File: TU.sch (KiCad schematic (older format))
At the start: 8 parts

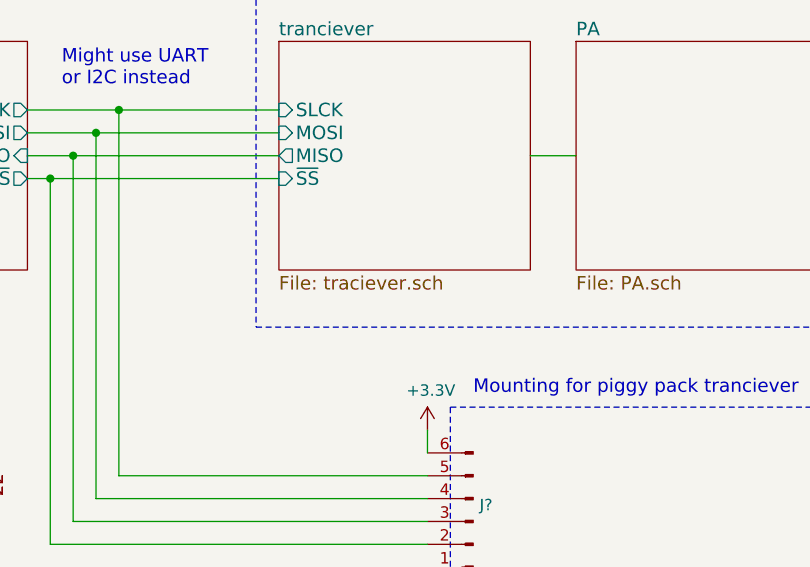
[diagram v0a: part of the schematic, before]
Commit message: Imported CAN and PSU blocks from infrastructure rep
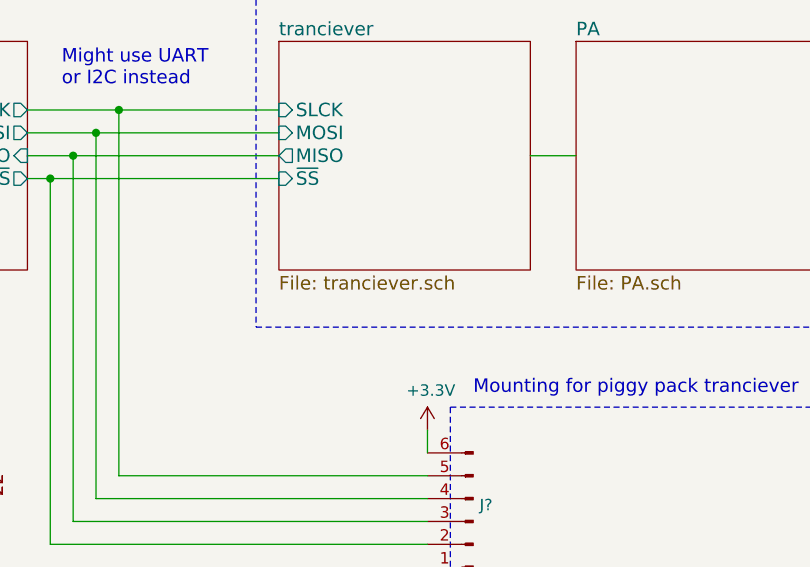
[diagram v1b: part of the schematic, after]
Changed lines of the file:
@@
 EESchema Schematic File Version 4
+LIBS:TU-cache
 EELAYER 30 0
 EELAYER END
@@
 $EndComp
 $Sheet
-S 6000 3000 1100 1000
-U 60144969
-F0 "tranciever" 59
-F1 "traciever.sch" 59
-F2 "SLCK" I L 6000 3300 59
-F3 "MOSI" I L 6000 3400 59
-F4 "MISO" O L 6000 3500 59
-F5 "~SS" I L 6000 3600 59
-$EndSheet
-$Sheet
 S 7300 3000 1100 1000
 U 60144AA2
@@
 Wire Wire Line
 	5100 3500 4900 3500
-Connection ~ 5000 3600
 Wire Wire Line
 	5000 3600 4900 3600
@@
 Wire Wire Line
 	5100 3500 6000 3500
-Wire Wire Line
-	5000 3600 6000 3600
 Wire Notes Line
 	5900 2650 5900 4250
@@
 Wire Notes Line
 	5900 2650 8550 2650
+$Sheet
+S 6000 3000 1100 1000
+U 60144374
+F0 "tranciever" 59
+F1 "tranciever.sch" 59
+F2 "SLCK" I L 6000 3300 59
+F3 "MOSI" I L 6000 3400 59
+F4 "MISO" O L 6000 3500 59
+F5 "~SS" I L 6000 3600 59
+$EndSheet
 Text Notes 5900 2600 0    59   ~ 0
 RF front end\n
+Connection ~ 5000 3600
+Wire Wire Line
+	5000 3600 6000 3600
 $EndSCHEMATC

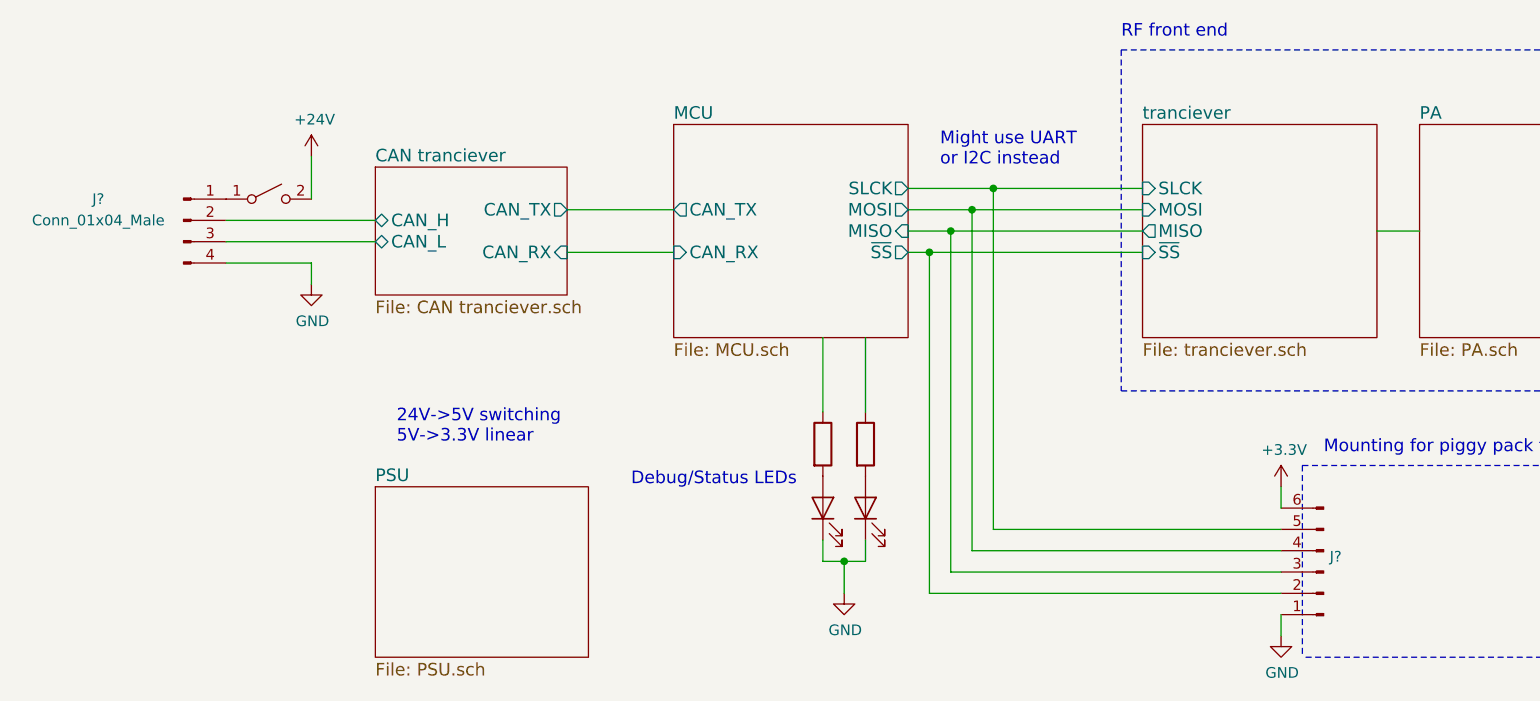
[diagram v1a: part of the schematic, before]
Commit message: Fixed weird hierarchical sheets
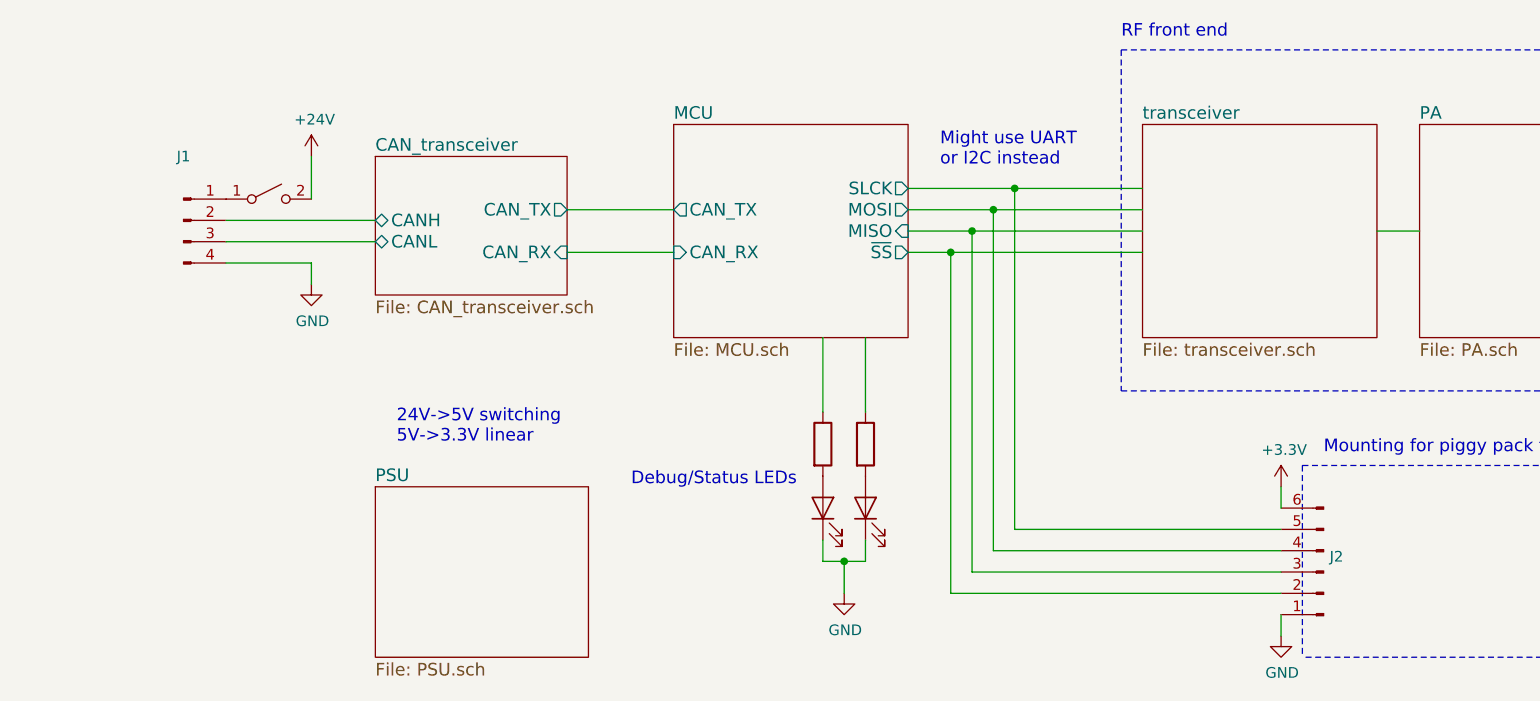
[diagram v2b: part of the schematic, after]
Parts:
- gave numbers to parts that had none: 8
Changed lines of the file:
@@
 	9100 3500 9100 3300
 $Comp
-L Device:Antenna AE?
+L Device:Antenna AE1
 U 1 1 60144042
 P 9100 3100
-F 0 "AE?" H 9180 3089 50  0001 L CNN
+F 0 "AE1" H 9180 3089 50  0001 L CNN
 F 1 "Antenna" H 9180 3043 50  0000 L CNN
 F 2 "" H 9100 3100 50  0001 C CNN
@@
 	1    0    0    -1
 $EndComp
-$Sheet
-S 7300 3000 1100 1000
-U 60144AA2
-F0 "PA" 59
-F1 "PA.sch" 59
-$EndSheet
 $Sheet
 S 3800 3000 1100 1000
@@
 F7 "CAN_RX" I L 3800 3600 59
 $EndSheet
-$Sheet
-S 2400 3200 900  600
-U 601450C1
-F0 "CAN tranciever" 59
-F1 "CAN tranciever.sch" 59
-F2 "CAN_H" B L 2400 3450 59
-F3 "CAN_L" B L 2400 3550 59
-F4 "CAN_TX" O R 3300 3400 59
-F5 "CAN_RX" I R 3300 3600 59
-$EndSheet
 Wire Wire Line
 	3300 3400 3800 3400
@@
 $EndSheet
 $Comp
-L Connector:Conn_01x04_Male J?
+L Connector:Conn_01x04_Male J1
 U 1 1 60145E85
 P 1500 3450
-F 0 "J?" H 1100 3550 50  0000 C CNN
-F 1 "Conn_01x04_Male" H 1100 3450 50  0000 C CNN
+F 0 "J1" H 1500 3750 50  0000 C CNN
+F 1 "Conn_01x04_Male" H 1100 3450 50  0001 C CNN
 F 2 "" H 1500 3450 50  0001 C CNN
 F 3 "~" H 1500 3450 50  0001 C CNN
@@
 $EndComp
 $Comp
-L Connector:Conn_01x06_Male J?
+L Connector:Conn_01x06_Male J2
 U 1 1 601485C2
 P 6850 5100
-F 0 "J?" H 6822 5028 50  0000 R CNN
+F 0 "J2" H 6822 5028 50  0000 R CNN
 F 1 "Conn_01x06_Male" H 6822 5073 50  0001 R CNN
 F 2 "" H 6850 5100 50  0001 C CNN
@@
 Text Notes 6850 4550 0    59   ~ 0
 Mounting for piggy pack tranciever
-Wire Wire Line
-	4900 3300 5300 3300
-Connection ~ 5300 3300
-Connection ~ 5200 3400
-Wire Wire Line
-	5200 3400 4900 3400
-Connection ~ 5100 3500
-Wire Wire Line
-	5100 3500 4900 3500
-Wire Wire Line
-	5000 3600 4900 3600
-$Comp
-L power:GND #PWR?
+$Comp
+L power:GND #PWR0101
 U 1 1 6014B5F8
 P 6650 5400
-F 0 "#PWR?" H 6650 5150 50  0001 C CNN
+F 0 "#PWR0101" H 6650 5150 50  0001 C CNN
 F 1 "GND" H 6655 5227 50  0000 C CNN
 F 2 "" H 6650 5400 50  0001 C CNN
@@
 $EndComp
 $Comp
-L power:+3.3V #PWR?
+L power:+3.3V #PWR0102
 U 1 1 6014B909
 P 6650 4700
-F 0 "#PWR?" H 6650 4550 50  0001 C CNN
+F 0 "#PWR0102" H 6650 4550 50  0001 C CNN
 F 1 "+3.3V" H 6665 4873 50  0000 C CNN
 F 2 "" H 6650 4700 50  0001 C CNN
@@
 	8400 3500 9100 3500
 Wire Wire Line
-	5300 3300 5300 4900
-Wire Wire Line
-	5300 4900 6650 4900
-Wire Wire Line
-	5200 3400 5200 5000
-Wire Wire Line
-	5200 5000 6650 5000
-Wire Wire Line
-	5100 3500 5100 5100
-Wire Wire Line
-	5100 5100 6650 5100
-Wire Wire Line
-	5000 5200 6650 5200
-Wire Wire Line
-	5000 3600 5000 5200
-$Comp
-L power:+24V #PWR?
+	5400 3300 5400 4900
+$Comp
+L power:+24V #PWR0103
 U 1 1 6015CE4B
 P 2100 3150
-F 0 "#PWR?" H 2100 3000 50  0001 C CNN
+F 0 "#PWR0103" H 2100 3000 50  0001 C CNN
 F 1 "+24V" H 2115 3323 50  0000 C CNN
 F 2 "" H 2100 3150 50  0001 C CNN
@@
 	2100 3650 2100 3750
 $Comp
-L power:GND #PWR?
+L power:GND #PWR0104
 U 1 1 6015D658
 P 2100 3750
-F 0 "#PWR?" H 2100 3500 50  0001 C CNN
+F 0 "#PWR0104" H 2100 3500 50  0001 C CNN
 F 1 "GND" H 2105 3577 50  0000 C CNN
 F 2 "" H 2100 3750 50  0001 C CNN
@@
 Debug/Status LEDs
 $Comp
-L power:GND #PWR?
+L power:GND #PWR0105
 U 1 1 6016E9C7
 P 4600 5200
-F 0 "#PWR?" H 4600 4950 50  0001 C CNN
+F 0 "#PWR0105" H 4600 4950 50  0001 C CNN
 F 1 "GND" H 4605 5027 50  0000 C CNN
 F 2 "" H 4600 5200 50  0001 C CNN
@@
 $EndComp
 $Comp
-L Device:LED D?
+L Device:LED D1
 U 1 1 601771CD
 P 4500 4800
-F 0 "D?" V 4539 4683 50  0001 R CNN
+F 0 "D1" V 4539 4683 50  0001 R CNN
 F 1 "LED" V 4448 4683 50  0001 R CNN
 F 2 "" H 4500 4800 50  0001 C CNN
@@
 $EndComp
 $Comp
-L Device:LED D?
+L Device:LED D2
 U 1 1 601777B4
 P 4700 4800
-F 0 "D?" V 4739 4683 50  0001 R CNN
+F 0 "D2" V 4739 4683 50  0001 R CNN
 F 1 "LED" V 4648 4683 50  0001 R CNN
 F 2 "" H 4700 4800 50  0001 C CNN
@@
 $EndComp
 $Comp
-L Device:R R?
+L Device:R R1
 U 1 1 60178366
 P 4500 4500
-F 0 "R?" H 4570 4546 50  0001 L CNN
+F 0 "R1" H 4570 4546 50  0001 L CNN
 F 1 "R" H 4570 4455 50  0001 L CNN
 F 2 "" V 4430 4500 50  0001 C CNN
@@
 $EndComp
 $Comp
-L Device:R R?
+L Device:R R2
 U 1 1 601786A2
 P 4700 4500
-F 0 "R?" H 4770 4546 50  0001 L CNN
+F 0 "R2" H 4770 4546 50  0001 L CNN
 F 1 "R" H 4770 4455 50  0001 L CNN
 F 2 "" V 4630 4500 50  0001 C CNN
@@
 	4500 4000 4500 4350
 $Comp
-L Switch:SW_DPST_x2 SW?
+L Switch:SW_DPST_x2 SW1
 U 1 1 6018598A
 P 1900 3350
-F 0 "SW?" H 1900 3585 50  0001 C CNN
+F 0 "SW1" H 1900 3585 50  0001 C CNN
 F 1 "SW_DPST_x2" H 1900 3494 50  0001 C CNN
 F 2 "" H 1900 3350 50  0000 C CNN
@@
 Wire Wire Line
 	7100 3500 7300 3500
-Wire Wire Line
-	5300 3300 6000 3300
-Wire Wire Line
-	5200 3400 6000 3400
-Wire Wire Line
-	5100 3500 6000 3500
 Wire Notes Line
 	5900 2650 5900 4250
@@
 Wire Notes Line
 	5900 2650 8550 2650
-$Sheet
-S 6000 3000 1100 1000
-U 60144374
-F0 "tranciever" 59
-F1 "tranciever.sch" 59
-F2 "SLCK" I L 6000 3300 59
-F3 "MOSI" I L 6000 3400 59
-F4 "MISO" O L 6000 3500 59
-F5 "~SS" I L 6000 3600 59
-$EndSheet
 Text Notes 5900 2600 0    59   ~ 0
 RF front end\n
-Connection ~ 5000 3600
-Wire Wire Line
-	5000 3600 6000 3600
+$Sheet
+S 6000 3000 1100 1000
+U 60145F44
+F0 "transceiver" 59
+F1 "transceiver.sch" 59
+$EndSheet
+$Sheet
+S 7300 3000 1100 1000
+U 6014566F
+F0 "PA" 59
+F1 "PA.sch" 59
+$EndSheet
+$Sheet
+S 2400 3150 900  650
+U 60145813
+F0 "CAN_transceiver" 59
+F1 "CAN_transceiver.sch" 59
+F2 "CAN_TX" O R 3300 3400 59
+F3 "CAN_RX" I R 3300 3600 59
+F4 "CANH" B L 2400 3450 59
+F5 "CANL" B L 2400 3550 59
+$EndSheet
+Connection ~ 5100 3600
+Wire Wire Line
+	5100 3600 6000 3600
+Wire Wire Line
+	5100 5200 6650 5200
+Connection ~ 5200 3500
+Wire Wire Line
+	5200 3500 6000 3500
+Wire Wire Line
+	5200 5100 6650 5100
+Connection ~ 5300 3400
+Wire Wire Line
+	5300 3400 6000 3400
+Wire Wire Line
+	5300 5000 6650 5000
+Connection ~ 5400 3300
+Wire Wire Line
+	5400 3300 6000 3300
+Wire Wire Line
+	5400 4900 6650 4900
+Wire Wire Line
+	4900 3300 5400 3300
+Wire Wire Line
+	4900 3400 5300 3400
+Wire Wire Line
+	4900 3500 5200 3500
+Wire Wire Line
+	4900 3600 5100 3600
+Wire Wire Line
+	5100 3600 5100 5200
+Wire Wire Line
+	5200 3500 5200 5100
+Wire Wire Line
+	5300 3400 5300 5000
 $EndSCHEMATC

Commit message: Added cc1190 reference design
also changed cc1190 symbol
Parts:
- removed AE1: Antenna, symbol Device:Antenna
- added J3: Conn_Coaxial, symbol Connector:Conn_Coaxial
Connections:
- wire segments 35 -> 33
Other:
- note added: "SMA antenna connector"
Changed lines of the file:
@@
 Comment4 ""
 $EndDescr
-Wire Wire Line
-	9100 3500 9100 3300
-$Comp
-L Device:Antenna AE1
-U 1 1 60144042
-P 9100 3100
-F 0 "AE1" H 9180 3089 50  0001 L CNN
-F 1 "Antenna" H 9180 3043 50  0000 L CNN
-F 2 "" H 9100 3100 50  0001 C CNN
-F 3 "~" H 9100 3100 50  0001 C CNN
-	1    9100 3100
-	1    0    0    -1
-$EndComp
 $Sheet
 S 3800 3000 1100 1000
@@
 Text Notes 5050 3200 0    59   ~ 0
 Might use UART \nor I2C instead
-Wire Wire Line
-	7100 3500 7300 3500
 Wire Notes Line
 	5900 2650 5900 4250
@@
 S 7300 3000 1100 1000
 U 6014566F
-F0 "PA" 59
+F0 "CC1190" 59
 F1 "PA.sch" 59
+F2 "HGM" I L 7300 3250 39
+F3 "LNA_EN" I L 7300 3350 39
+F4 "PA_EN" I L 7300 3450 39
+F5 "RFIO" B L 7300 3550 39
+F6 "ANTENNA_OUT" O R 8400 3500 39
 $EndSheet
 $Sheet
@@
 Wire Wire Line
 	5300 3400 5300 5000
+$Comp
+L Connector:Conn_Coaxial J3
+U 1 1 60221CCA
+P 9300 3500
+F 0 "J3" H 9400 3475 50  0000 L CNN
+F 1 "Conn_Coaxial" H 9400 3384 50  0000 L CNN
+F 2 "" H 9300 3500 50  0001 C CNN
+F 3 " ~" H 9300 3500 50  0001 C CNN
+	1    9300 3500
+	1    0    0    -1
+$EndComp
+$Comp
+L power:GND #PWR01
+U 1 1 60222AF8
+P 9300 3700
+F 0 "#PWR01" H 9300 3450 50  0001 C CNN
+F 1 "GND" H 9305 3527 50  0000 C CNN
+F 2 "" H 9300 3700 50  0001 C CNN
+F 3 "" H 9300 3700 50  0001 C CNN
+	1    9300 3700
+	1    0    0    -1
+$EndComp
+Text Notes 8850 3300 0    59   ~ 0
+SMA antenna connector
 $EndSCHEMATC

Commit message: Started work on CC1200
might not be actual final tranciever
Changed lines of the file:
@@
 F3 "MOSI" O R 4900 3400 59
 F4 "MISO" I R 4900 3500 59
-F5 "~SS" O R 4900 3600 59
-F6 "CAN_TX" O L 3800 3400 59
-F7 "CAN_RX" I L 3800 3600 59
+F5 "CAN_TX" O L 3800 3400 59
+F6 "CAN_RX" I L 3800 3600 59
+F7 "~CS" O R 4900 3600 59
 $EndSheet
 Wire Wire Line

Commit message: Started work on MCU
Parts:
- removed D1, D2: LED, symbol Device:LED
- removed J1: Conn_01x04_Male, symbol Connector:Conn_01x04_Male
- removed R1, R2: R, symbol Device:R
- added J1: Conn_01x06_Male, symbol Connector:Conn_01x06_Male
- added J4: Debugger, symbol Connector_Generic:Conn_02x05_Odd_Even
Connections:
- wire segments 33 -> 51
- no-connect marks 0 -> 2
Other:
- note removed: "Debug/Status LEDs"
- moved on the sheet: J2

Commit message: More work on tranciever and PA
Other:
- note removed: "Might use UART \nor I2C instead"
- moved on the sheet: J1, J2, J3, J4
